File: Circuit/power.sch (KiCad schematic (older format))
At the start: 20 parts, among them Q202 FDN340P, Q203 FDN340P, SW1 ON/OFF, U201 CN3063, U202 MCP6002, U3 LXDC2XQ

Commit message: Added EC11 Rotary Encoder footprint
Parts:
- C12: footprint (none) -> Capacitors_SMD:C_0603_HandSoldering
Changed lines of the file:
@@
 USB_IN
 $Comp
-L GND #PWR32
+L GND #PWR032
 U 1 1 563C4E24
 P 3950 4650
-F 0 "#PWR32" H 3950 4400 50  0001 C CNN
+F 0 "#PWR032" H 3950 4400 50  0001 C CNN
 F 1 "GND" H 3950 4500 50  0000 C CNN
 F 2 "" H 3950 4650 60  0000 C CNN
@@
 Charging current\nIr = 252mA max
 $Comp
-L GND #PWR35
+L GND #PWR033
 U 1 1 56417FB3
 P 7450 4200
-F 0 "#PWR35" H 7450 3950 50  0001 C CNN
+F 0 "#PWR033" H 7450 3950 50  0001 C CNN
 F 1 "GND" H 7450 4050 50  0000 C CNN
 F 2 "" H 7450 4200 60  0000 C CNN
@@
 3.3OUT
 $Comp
-L GND #PWR40
+L GND #PWR034
 U 1 1 5641AA9F
 P 10250 2500
-F 0 "#PWR40" H 10250 2250 50  0001 C CNN
+F 0 "#PWR034" H 10250 2250 50  0001 C CNN
 F 1 "GND" H 10250 2350 50  0000 C CNN
 F 2 "" H 10250 2500 60  0000 C CNN
@@
 $EndComp
 $Comp
-L GND #PWR36
+L GND #PWR035
 U 1 1 5642C1C1
 P 9050 4100
-F 0 "#PWR36" H 9050 3850 50  0001 C CNN
+F 0 "#PWR035" H 9050 3850 50  0001 C CNN
 F 1 "GND" H 9050 3950 50  0000 C CNN
 F 2 "" H 9050 4100 60  0000 C CNN
@@
 $EndComp
 $Comp
-L PWR_FLAG #FLG2
+L PWR_FLAG #FLG036
 U 1 1 5642D1CE
 P 10450 1800
-F 0 "#FLG2" H 10450 1895 50  0001 C CNN
+F 0 "#FLG036" H 10450 1895 50  0001 C CNN
 F 1 "PWR_FLAG" H 10450 1980 50  0000 C CNN
 F 2 "" H 10450 1800 60  0000 C CNN
@@
 $EndComp
 $Comp
-L PWR_FLAG #FLG1
+L PWR_FLAG #FLG037
 U 1 1 5642D5A3
 P 3900 1800
-F 0 "#FLG1" H 3900 1895 50  0001 C CNN
+F 0 "#FLG037" H 3900 1895 50  0001 C CNN
 F 1 "PWR_FLAG" H 3900 1980 50  0000 C CNN
 F 2 "" H 3900 1800 60  0000 C CNN
@@
 $EndComp
 $Comp
-L GND #PWR39
+L GND #PWR038
 U 1 1 5642DA26
 P 10000 4150
-F 0 "#PWR39" H 10000 3900 50  0001 C CNN
+F 0 "#PWR038" H 10000 3900 50  0001 C CNN
 F 1 "GND" H 10000 4000 50  0000 C CNN
 F 2 "" H 10000 4150 60  0000 C CNN
@@
 $EndComp
 $Comp
-L GND #PWR33
+L GND #PWR039
 U 1 1 5642CE9D
 P 4600 2350
-F 0 "#PWR33" H 4600 2100 50  0001 C CNN
+F 0 "#PWR039" H 4600 2100 50  0001 C CNN
 F 1 "GND" H 4600 2200 50  0000 C CNN
 F 2 "" H 4600 2350 60  0000 C CNN
@@
 $EndComp
 $Comp
-L GND #PWR34
+L GND #PWR040
 U 1 1 566FA00B
 P 6300 3100
-F 0 "#PWR34" H 6300 2850 50  0001 C CNN
+F 0 "#PWR040" H 6300 2850 50  0001 C CNN
 F 1 "GND" H 6300 2950 50  0000 C CNN
 F 2 "" H 6300 3100 60  0000 C CNN
@@
 $EndComp
 $Comp
-L GND #PWR37
+L GND #PWR041
 U 1 1 5812C93A
 P 9500 6300
-F 0 "#PWR37" H 9500 6050 50  0001 C CNN
+F 0 "#PWR041" H 9500 6050 50  0001 C CNN
 F 1 "GND" H 9500 6150 50  0000 C CNN
 F 2 "" H 9500 6300 60  0000 C CNN
@@
 $EndComp
 $Comp
-L GND #PWR38
+L GND #PWR042
 U 1 1 5812E212
 P 9800 5000
-F 0 "#PWR38" H 9800 4750 50  0001 C CNN
+F 0 "#PWR042" H 9800 4750 50  0001 C CNN
 F 1 "GND" H 9800 4850 50  0000 C CNN
 F 2 "" H 9800 5000 60  0000 C CNN
@@
 F 0 "C12" H 10500 6000 50  0000 L CNN
 F 1 "10uF" H 10500 5800 50  0000 L CNN
-F 2 "" H 10450 5900 60  0000 C CNN
+F 2 "Capacitors_SMD:C_0603_HandSoldering" H 10450 5900 60  0001 C CNN
 F 3 "" H 10450 5900 60  0000 C CNN
 	1    10450 5900

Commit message: Moved LXDC2XQ location
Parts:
- U3: footprint IoTuz:LXDC2XQ -> libs:LXDC2XQ
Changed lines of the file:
@@
 F 0 "U3" H 8950 5950 60  0000 C CNN
 F 1 "LXDC2XQ" H 10000 5150 60  0000 C CNN
-F 2 "IoTuz:LXDC2XQ" H 9500 5550 60  0001 C CNN
+F 2 "libs:LXDC2XQ" H 9500 5550 60  0001 C CNN
 F 3 "http://power.murata.com/data/power/LXDC2XQ_Series_datasheet.pdf" H 9500 5550 60  0001 C CNN
 F 4 "Digikey" H 9500 5550 60  0001 C CNN "Supplier"

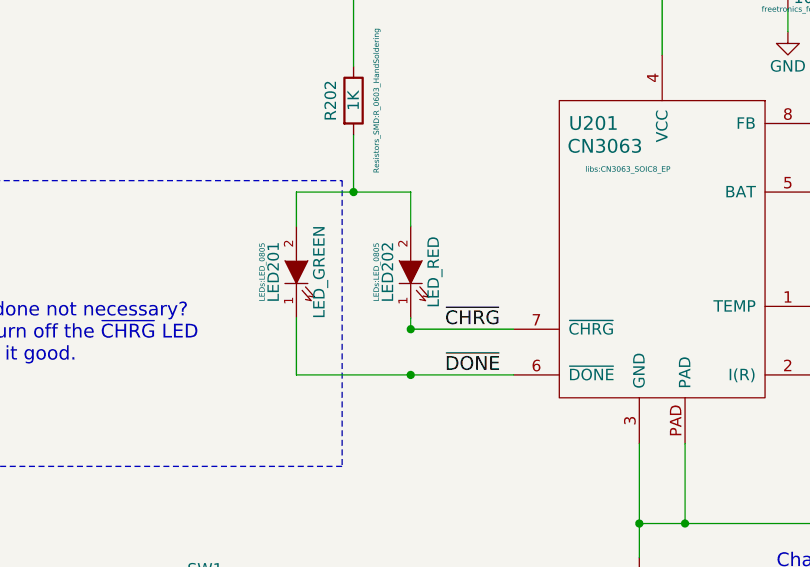
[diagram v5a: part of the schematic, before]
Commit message: Removed PRGM button. placed some components.
PGRM button can be performed by joystick.
CHRG led removed.
placed some components.
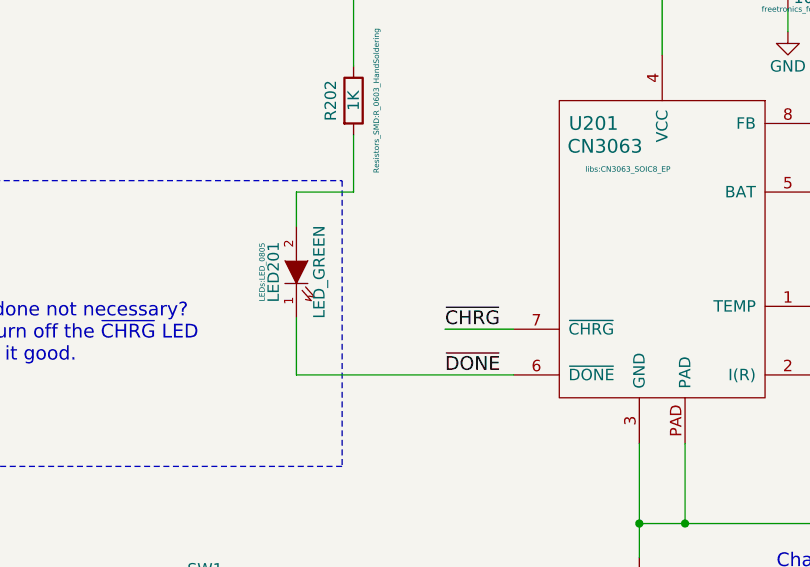
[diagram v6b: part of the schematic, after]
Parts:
- removed LED202: LED_RED, LEDs:LED_0805, symbol LED
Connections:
- wire segments 77 -> 75
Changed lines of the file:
@@
 USB_IN
 $Comp
-L GND #PWR032
+L GND #PWR031
 U 1 1 563C4E24
 P 3950 4650
-F 0 "#PWR032" H 3950 4400 50  0001 C CNN
+F 0 "#PWR031" H 3950 4400 50  0001 C CNN
 F 1 "GND" H 3950 4500 50  0000 C CNN
 F 2 "" H 3950 4650 60  0000 C CNN
@@
 	1    2200 1800
 	1    0    0    -1
-$EndComp
-$Comp
-L LED LED202
-U 1 1 563C5FC4
-P 2950 3400
-F 0 "LED202" H 2950 3500 50  0000 C CNN
-F 1 "LED_RED" H 2950 3300 50  0000 C CNN
-F 2 "LEDs:LED_0805" H 2950 3550 24  0000 C CNN
-F 3 "" H 2950 3400 60  0000 C CNN
-	1    2950 3400
-	0    -1   -1   0
 $EndComp
 Text Label 5300 1800 0    60   ~ 0
@@
 Charging current\nIr = 252mA max
 $Comp
-L GND #PWR033
+L GND #PWR032
 U 1 1 56417FB3
 P 7450 4200
-F 0 "#PWR033" H 7450 3950 50  0001 C CNN
+F 0 "#PWR032" H 7450 3950 50  0001 C CNN
 F 1 "GND" H 7450 4050 50  0000 C CNN
 F 2 "" H 7450 4200 60  0000 C CNN
@@
 3.3OUT
 $Comp
-L GND #PWR034
+L GND #PWR033
 U 1 1 5641AA9F
 P 10250 2500
-F 0 "#PWR034" H 10250 2250 50  0001 C CNN
+F 0 "#PWR033" H 10250 2250 50  0001 C CNN
 F 1 "GND" H 10250 2350 50  0000 C CNN
 F 2 "" H 10250 2500 60  0000 C CNN
@@
 $EndComp
 $Comp
-L GND #PWR035
+L GND #PWR034
 U 1 1 5642C1C1
 P 9050 4100
-F 0 "#PWR035" H 9050 3850 50  0001 C CNN
+F 0 "#PWR034" H 9050 3850 50  0001 C CNN
 F 1 "GND" H 9050 3950 50  0000 C CNN
 F 2 "" H 9050 4100 60  0000 C CNN
@@
 $EndComp
 $Comp
-L PWR_FLAG #FLG036
+L PWR_FLAG #FLG035
 U 1 1 5642D1CE
 P 10450 1800
-F 0 "#FLG036" H 10450 1895 50  0001 C CNN
+F 0 "#FLG035" H 10450 1895 50  0001 C CNN
 F 1 "PWR_FLAG" H 10450 1980 50  0000 C CNN
 F 2 "" H 10450 1800 60  0000 C CNN
@@
 $EndComp
 $Comp
-L PWR_FLAG #FLG037
+L PWR_FLAG #FLG036
 U 1 1 5642D5A3
 P 3900 1800
-F 0 "#FLG037" H 3900 1895 50  0001 C CNN
+F 0 "#FLG036" H 3900 1895 50  0001 C CNN
 F 1 "PWR_FLAG" H 3900 1980 50  0000 C CNN
 F 2 "" H 3900 1800 60  0000 C CNN
@@
 $EndComp
 $Comp
-L GND #PWR038
+L GND #PWR037
 U 1 1 5642DA26
 P 10000 4150
-F 0 "#PWR038" H 10000 3900 50  0001 C CNN
+F 0 "#PWR037" H 10000 3900 50  0001 C CNN
 F 1 "GND" H 10000 4000 50  0000 C CNN
 F 2 "" H 10000 4150 60  0000 C CNN
@@
 $EndComp
 $Comp
-L GND #PWR039
+L GND #PWR038
 U 1 1 5642CE9D
 P 4600 2350
-F 0 "#PWR039" H 4600 2100 50  0001 C CNN
+F 0 "#PWR038" H 4600 2100 50  0001 C CNN
 F 1 "GND" H 4600 2200 50  0000 C CNN
 F 2 "" H 4600 2350 60  0000 C CNN
@@
 $EndComp
 $Comp
-L GND #PWR040
+L GND #PWR039
 U 1 1 566FA00B
 P 6300 3100
-F 0 "#PWR040" H 6300 2850 50  0001 C CNN
+F 0 "#PWR039" H 6300 2850 50  0001 C CNN
 F 1 "GND" H 6300 2950 50  0000 C CNN
 F 2 "" H 6300 3100 60  0000 C CNN
@@
 $EndComp
 $Comp
-L GND #PWR041
+L GND #PWR040
 U 1 1 5812C93A
 P 9500 6300
-F 0 "#PWR041" H 9500 6050 50  0001 C CNN
+F 0 "#PWR040" H 9500 6050 50  0001 C CNN
 F 1 "GND" H 9500 6150 50  0000 C CNN
 F 2 "" H 9500 6300 60  0000 C CNN
@@
 $EndComp
 $Comp
-L GND #PWR042
+L GND #PWR041
 U 1 1 5812E212
 P 9800 5000
-F 0 "#PWR042" H 9800 4750 50  0001 C CNN
+F 0 "#PWR041" H 9800 4750 50  0001 C CNN
 F 1 "GND" H 9800 4850 50  0000 C CNN
 F 2 "" H 9800 5000 60  0000 C CNN
@@
 	2400 1800 6650 1800
 Wire Wire Line
-	2950 3650 3400 3650
-Connection ~ 2950 3650
-Wire Wire Line
-	2950 3050 2950 3200
-Connection ~ 2950 3850
+	3100 3650 3400 3650
 Wire Wire Line
 	6850 2100 6850 3750
@@
 	5800 3750 5900 3750
 Wire Wire Line
-	2950 3600 2950 3650
-Wire Wire Line
 	5050 3050 4700 3050
 Connection ~ 5850 2750
@@
 	2700 2800 2700 3050
 Wire Wire Line
-	2450 3050 2950 3050
-Connection ~ 2700 3050
+	2700 3050 2450 3050
 Wire Wire Line
 	6300 2700 6300 2500

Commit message: Adding some component information, connecting audio.
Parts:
- U3: footprint libs:LXDC2XQ -> (none); Supplier Digikey -> (none); Unit Cost (1) 1.55 -> (none); Unit cost (none) -> 1.55
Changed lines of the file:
@@
 Charge done not necessary? \nI'd just turn off the ~CHRG~ LED\n and call it good.
-$Comp
-L LXDC2XQ U3
-U 1 1 5812C4CE
-P 9500 5550
-F 0 "U3" H 8950 5950 60  0000 C CNN
-F 1 "LXDC2XQ" H 10000 5150 60  0000 C CNN
-F 2 "libs:LXDC2XQ" H 9500 5550 60  0001 C CNN
-F 3 "http://power.murata.com/data/power/LXDC2XQ_Series_datasheet.pdf" H 9500 5550 60  0001 C CNN
-F 4 "Digikey" H 9500 5550 60  0001 C CNN "Supplier"
-F 5 "http://www.digikey.com.au/product-detail/en/murata-electronics-north-america/LXDC2XQ33A-254/490-12573-1-ND/5797558" H 9500 5550 60  0001 C CNN "Digikey URL"
-F 6 "1.55" H 9500 5550 60  0001 C CNN "Unit Cost (1)"
-F 7 "490-12573-1-ND" H 9500 5550 60  0001 C CNN "Digikey PN"
-	1    9500 5550
-	1    0    0    -1
-$EndComp
 $Comp
 L GND #PWR040
@@
 Wire Wire Line
 	10450 6200 9500 6200
+$Comp
+L LXDC2XQ U3
+U 1 1 581FF216
+P 9500 5550
+F 0 "U3" H 8950 5950 60  0000 C CNN
+F 1 "LXDC2XQ" H 10000 5150 60  0000 C CNN
+F 2 "" H 8850 5850 60  0001 C CNN
+F 3 "http://power.murata.com/data/power/LXDC2XQ_Series_datasheet.pdf" H 8950 5950 60  0001 C CNN
+F 4 "http://www.digikey.com.au/product-detail/en/murata-electronics-north-america/LXDC2XQ33A-254/490-12573-1-ND/5797558" H 9050 6050 60  0001 C CNN "Digikey URL"
+F 5 "1.55" H 9150 6150 60  0001 C CNN "Unit cost"
+F 6 "490-12573-1-ND" H 9250 6250 60  0001 C CNN "Digikey PN"
+	1    9500 5550
+	1    0    0    -1
+$EndComp
 $EndSCHEMATC

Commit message: More component information.
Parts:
- LED201: value LED_GREEN -> LED_PURPLE
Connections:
- net labels removed: ~DONE
- wire segments 75 -> 72
- no-connect marks 0 -> 1
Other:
- note removed: "Charge done not necessary? \nI'd just turn off the ~CHRG~ LED\n and call it good."
- moved on the sheet: LED201
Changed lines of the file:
@@
 L LED LED201
 U 1 1 563FF8B1
-P 2450 3400
-F 0 "LED201" H 2450 3500 50  0000 C CNN
-F 1 "LED_GREEN" H 2450 3300 50  0000 C CNN
-F 2 "LEDs:LED_0805" H 2450 3550 24  0000 C CNN
-F 3 "" H 2450 3400 60  0000 C CNN
-	1    2450 3400
+P 2700 3350
+F 0 "LED201" H 2700 3450 50  0000 C CNN
+F 1 "LED_PURPLE" H 2700 3250 50  0000 C CNN
+F 2 "LEDs:LED_0805" H 2700 3500 24  0000 C CNN
+F 3 "" H 2700 3350 60  0000 C CNN
+	1    2700 3350
 	0    -1   -1   0
 $EndComp
@@
 Text Label 3100 3650 0    60   ~ 0
 ~CHRG
-Text Label 3100 3850 0    60   ~ 0
-~DONE
 $Comp
 L MOSFET_P Q202
@@
 	1    0    0    -1
 $EndComp
-Text Notes 800  3800 0    60   ~ 0
-Charge done not necessary? \nI'd just turn off the ~CHRG~ LED\n and call it good.
 $Comp
 L GND #PWR040
@@
 	2400 1800 6650 1800
 Wire Wire Line
-	3100 3650 3400 3650
-Wire Wire Line
 	6850 2100 6850 3750
-Wire Wire Line
-	2450 3850 3400 3850
-Wire Wire Line
-	2450 3050 2450 3200
-Wire Wire Line
-	2450 3600 2450 3850
 Wire Wire Line
 	4950 4500 4950 4300
@@
 Connection ~ 2700 1800
 Wire Wire Line
-	2700 2800 2700 3050
-Wire Wire Line
-	2700 3050 2450 3050
+	2700 2800 2700 3150
 Wire Wire Line
 	6300 2700 6300 2500
@@
 Wire Wire Line
 	1650 1800 2000 1800
-Wire Notes Line
-	750  3000 2650 3000
-Wire Notes Line
-	2650 3000 2650 4250
-Wire Notes Line
-	2650 4250 750  4250
-Wire Notes Line
-	750  4250 750  3000
 Wire Wire Line
 	9350 6200 9650 6200
@@
 	1    0    0    -1
 $EndComp
+Wire Wire Line
+	2700 3550 2700 3650
+Wire Wire Line
+	2700 3650 3400 3650
+NoConn ~ 3400 3850
 $EndSCHEMATC
